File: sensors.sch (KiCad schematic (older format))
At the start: 12 parts

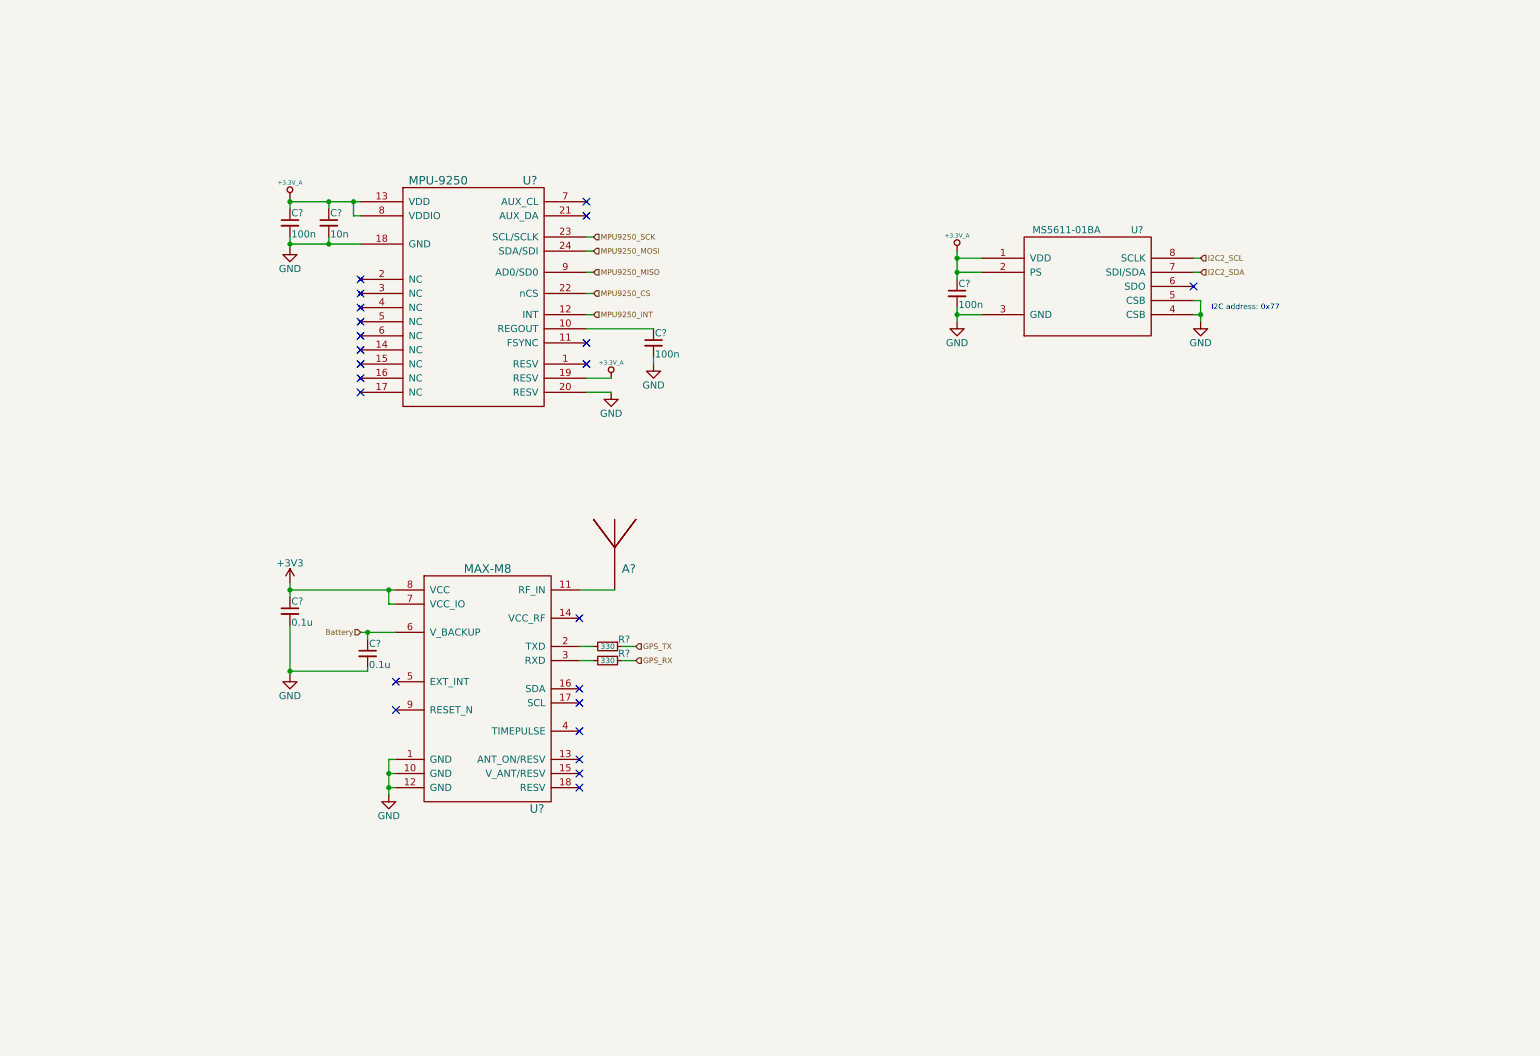
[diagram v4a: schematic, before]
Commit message: Schematics: Minor cleanups
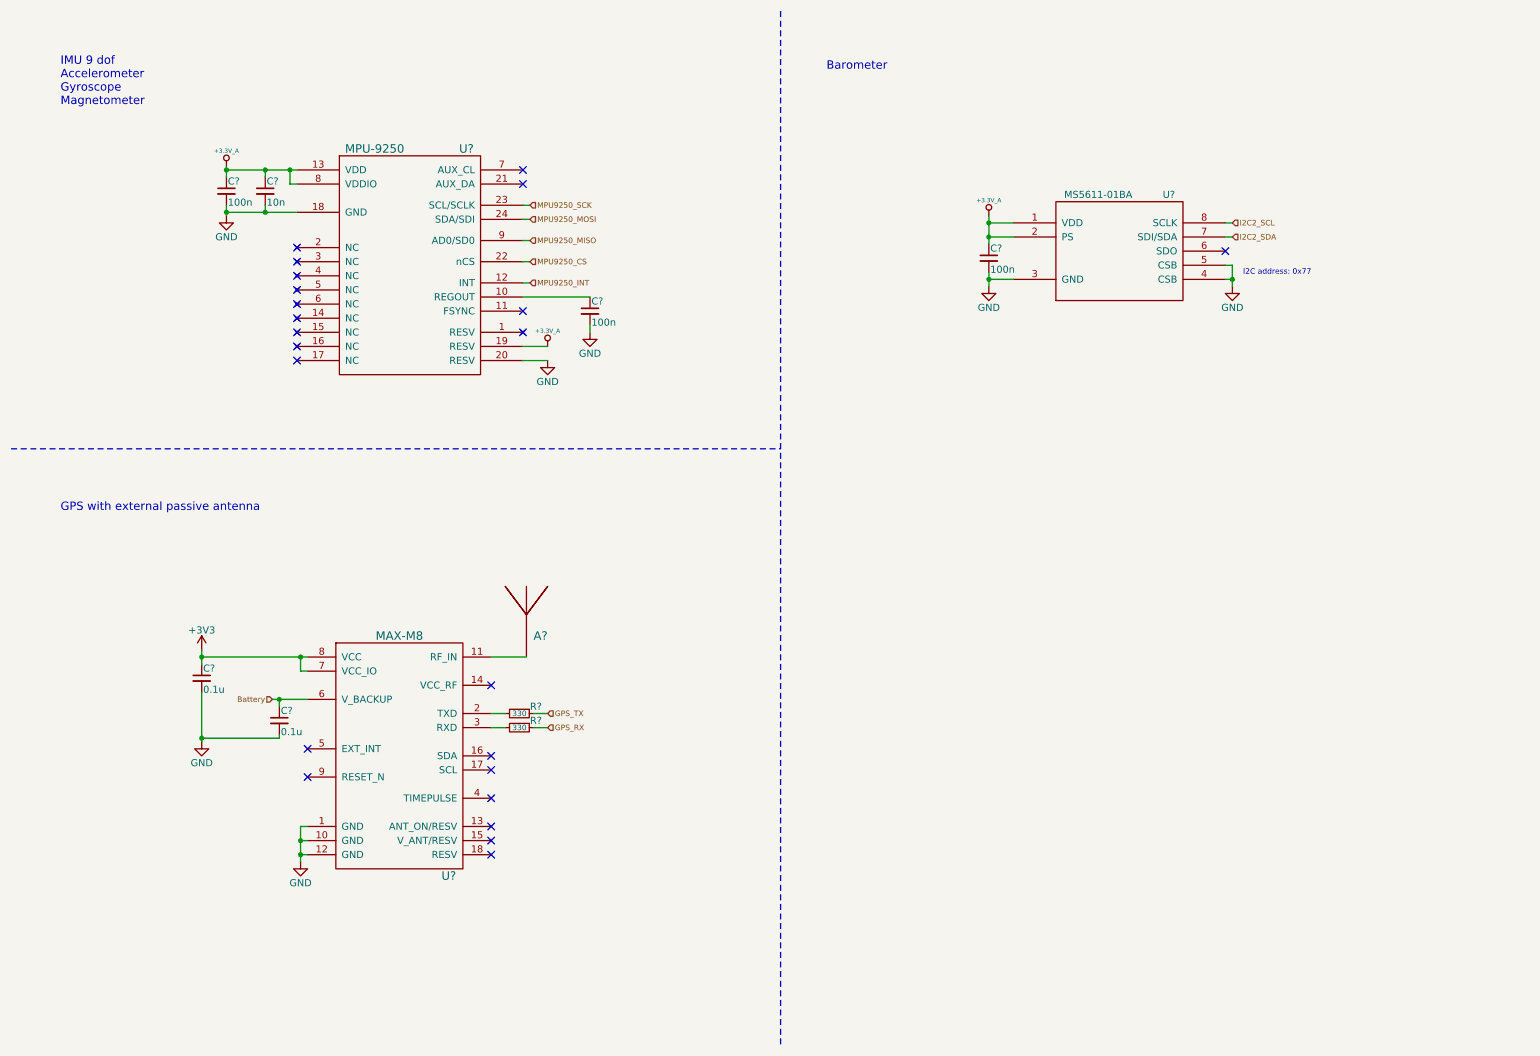
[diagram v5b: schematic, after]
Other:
- note added: "Barometer"
- note added: "GPS with external passive antenna"
- note added: "IMU 9 dof\nAccelerometer\nGyroscope\nMagnetometer"
- moved on the sheet: A?, C?, R?, U?

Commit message: Schematics: LEDs
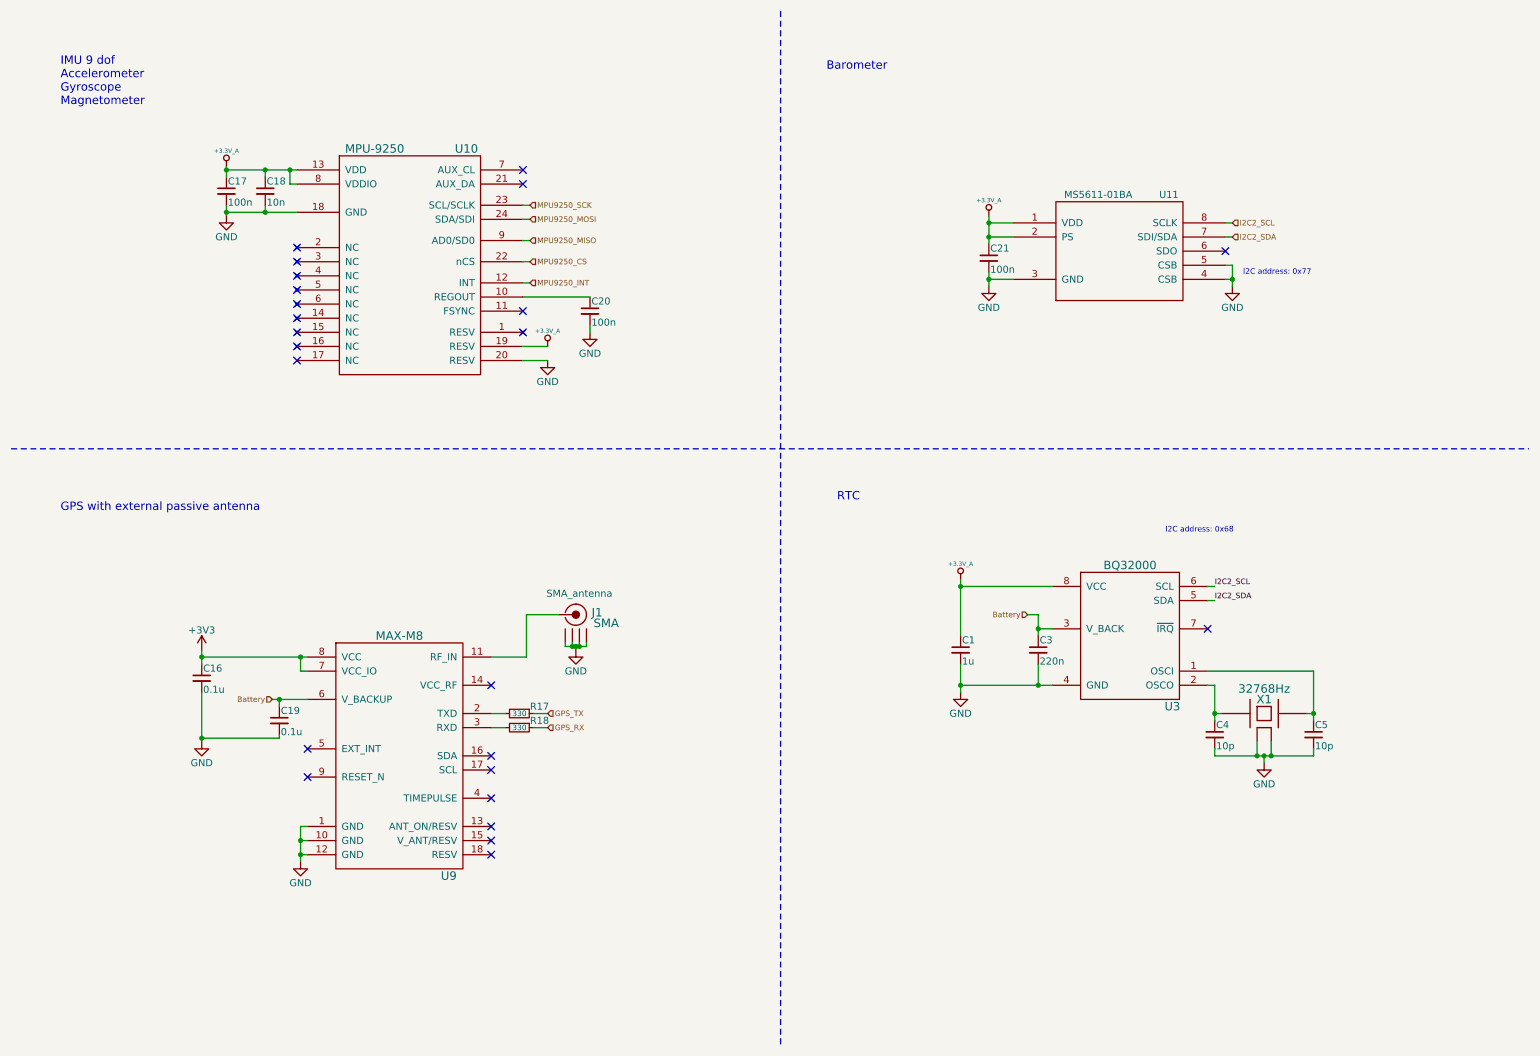
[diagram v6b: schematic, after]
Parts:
- removed A?: ANTENNA, symbol ANTENNA
- added C1: 1u, symbol C_Small
- added C3: 220n, symbol C_Small
- added C4, C5: 10p, symbol C_Small
- added J1: SMA, SMA_antenna, symbol SMA
- added U3: BQ32000, symbol BQ32000
- added X1: 32768Hz, symbol XTAL-SMD-4-PADS
- gave numbers to parts that had none: 11
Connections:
- net +3.3V_A: now also C1.1, U3.8 (VCC)
- net Battery: now also C3.1, U3.3 (V_BACK)
- net GND: now also C1.2, C3.2, C4.2, C5.2, J1.2 (GND1), J1.3 (GND2), J1.4 (GND3), J1.5 (GND4), U3.4 (GND), X1.2 (case), X1.4 (case)
- net I2C2_SCL: now also U3.6 (SCL)
- net I2C2_SDA: now also U3.5 (SDA)
- net at U9.11 (RF_IN): now also J1.1 (RF)
- new net: C5.1, U3.1 (OSCI), X1.3
- new net: C4.1, U3.2 (OSCO), X1.1
- no-connect marks 23 -> 24
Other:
- note added: "I2C address: 0x68"
- note added: "RTC"
